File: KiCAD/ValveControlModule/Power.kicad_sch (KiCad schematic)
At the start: 12 parts, among them U5 NCV8114BSN330T1G

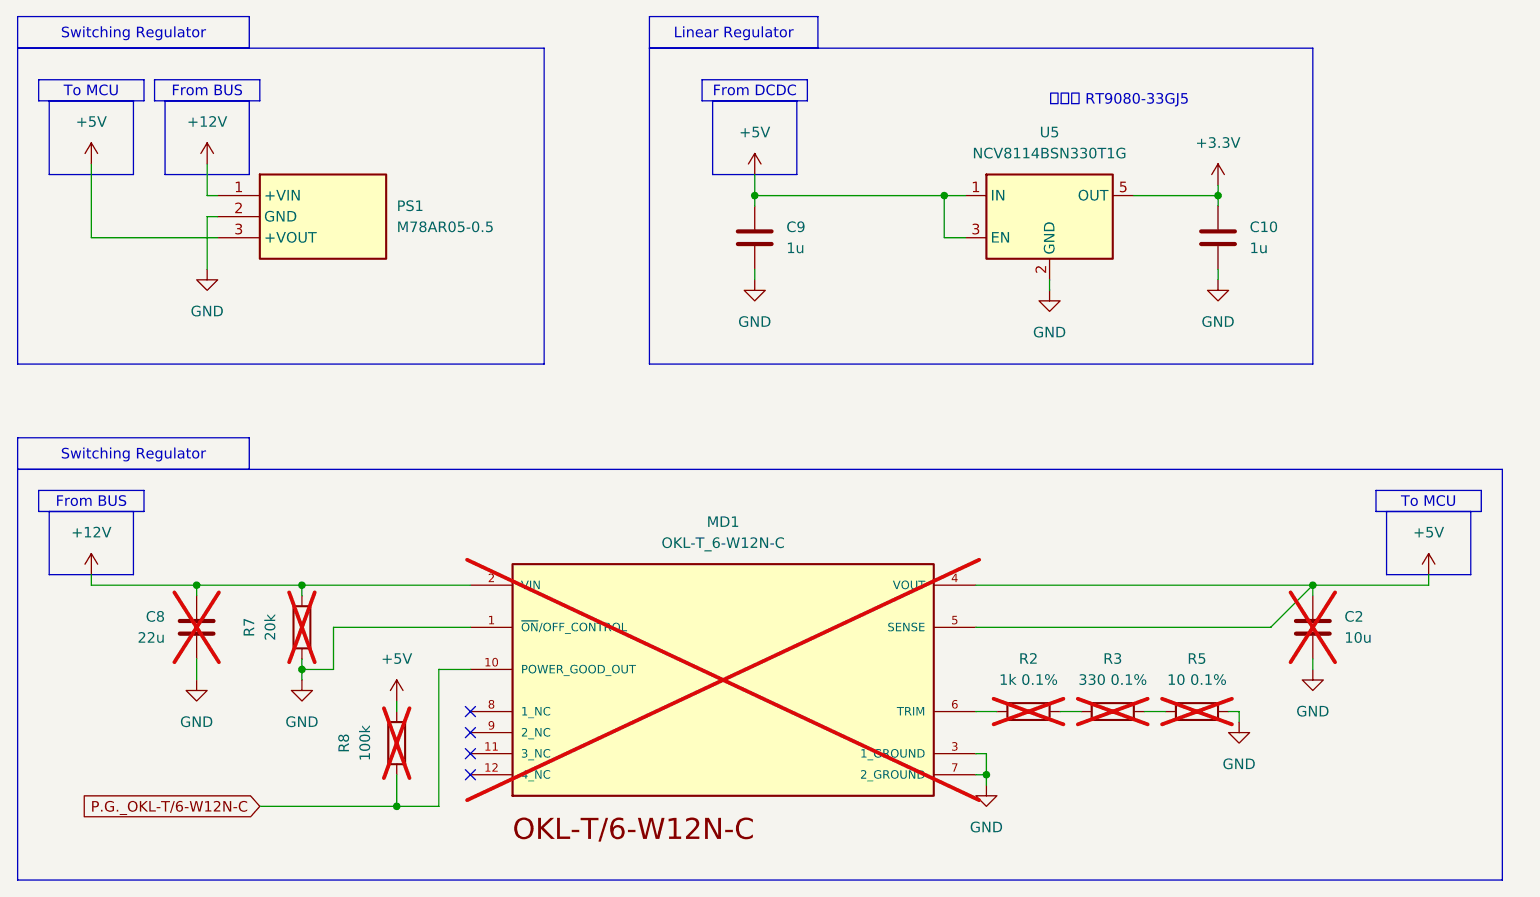
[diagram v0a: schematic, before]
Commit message: 取り付け穴位置を更新
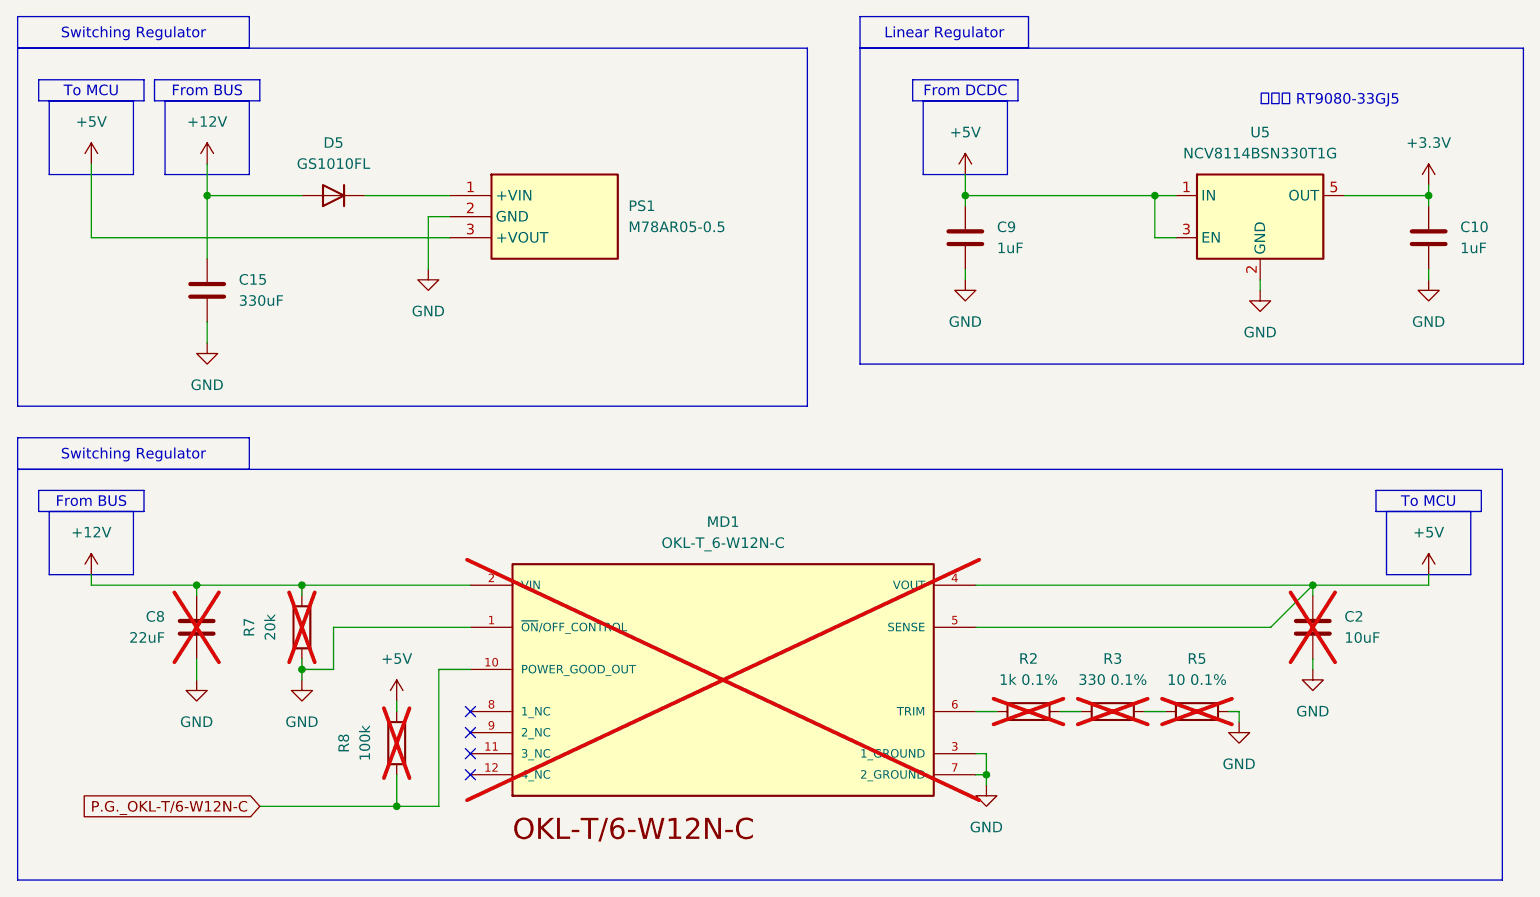
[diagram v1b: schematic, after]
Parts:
- added C15: 330uF, Capacitor_SMD:CP_Elec_10x10, symbol Device:C
- added D5: GS1010FL, Diode_SMD:D_SOD-123F, symbol Device:D
- C10, C9: value 1u -> 1uF
- C2: value 10u -> 10uF
- C8: value 22u -> 22uF
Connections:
- net +12V: now also C15.2, D5.2 (A); no longer PS1.1 (+VIN)
- net GND: now also C15.1
- new net: D5.1 (K), PS1.1 (+VIN)
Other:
- moved on the sheet: C10, C9, PS1, U5

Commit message: Build-2完成．発注．
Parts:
- removed D5: GS1010FL, Diode_SMD:D_SOD-123F, symbol Device:D
- added D9: SB34AFC, Diode_SMD:D_SMA_Handsoldering, symbol Device:D_Schottky
- C15: symbol Device:C -> Device:C_Polarized
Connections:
- net +12V: now also C15.1, D9.2 (A); no longer C15.2
- net GND: now also C15.2; no longer C15.1
- net at PS1.1 (+VIN): now also D9.1 (K)
